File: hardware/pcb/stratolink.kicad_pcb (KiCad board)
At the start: 2 copper layers, 23.4 x 57.3 mm, 61 parts, among them J1 Solar panel direct solder, J2 Solar panel direct solder, J20 Conn_ARM_SWD_TagConnect_TC203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, J3 Conn_PinHeader_1x07_P2.54mm_V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, J4 Conn_PinHeader_1x07_P2.54mm_V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, U2 RAK3172, U5 TMP117NAIYBGR, U7 LIS2DH12TR

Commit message: Prepare v1.1 pilot hardware and verified manufacturing draft
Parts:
- added C22: 100nF, lib:Stratolink_v1p1_C22_C_0402_1005Metric, B.Cu at (55.6, 38.3)
- added R24: 4.75MΩ, lib:Stratolink_v1p1_R24_R_0402_1005Metric, B.Cu at (57.4, 33.9)
- added R25: 4.75MΩ, lib:Stratolink_v1p1_R25_R_0402_1005Metric, B.Cu at (58.6, 34.9)
- added R26: 22Ω, lib:Stratolink_v1p1_R26_R_0402_1005Metric, B.Cu at (61.2, 42.5)
- added U8: TLV8801DBVT, lib:Stratolink_v1p1_U8_SOT-23-5, B.Cu at (55.6, 36.1)
- C1: footprint Capacitor_SMD:C_0402_1005Metric -> lib:Stratolink_v1p1_C1_C_0402_1005Metric
- C10: footprint Capacitor_SMD:C_0402_1005Metric -> lib:Stratolink_v1p1_C10_C_0402_1005Metric
- C11: footprint Capacitor_SMD:C_0402_1005Metric -> lib:Stratolink_v1p1_C11_C_0402_1005Metric
- C12: footprint Capacitor_SMD:C_0402_1005Metric -> lib:Stratolink_v1p1_C12_C_0402_1005Metric
- C14: footprint Capacitor_SMD:C_0402_1005Metric -> lib:Stratolink_v1p1_C14_C_0402_1005Metric
- C15: footprint Capacitor_SMD:C_0402_1005Metric -> lib:Stratolink_v1p1_C15_C_0402_1005Metric
- C16: footprint Capacitor_SMD:C_0603_1608Metric -> lib:Stratolink_v1p1_C16_C_0603_1608Metric
- C17: footprint Capacitor_SMD:C_0402_1005Metric -> lib:Stratolink_v1p1_C17_C_0402_1005Metric
- C19: footprint Capacitor_SMD:C_0402_1005Metric -> lib:Stratolink_v1p1_C19_C_0402_1005Metric
- C2: footprint Capacitor_SMD:C_0603_1608Metric -> lib:Stratolink_v1p1_C2_C_0603_1608Metric
- C20: footprint Capacitor_SMD:C_0402_1005Metric -> lib:Stratolink_v1p1_C20_C_0402_1005Metric
- C21: footprint Capacitor_SMD:C_0603_1608Metric -> lib:Stratolink_v1p1_C21_C_0603_1608Metric
- C3: footprint Capacitor_SMD:C_0603_1608Metric -> lib:Stratolink_v1p1_C3_C_0603_1608Metric
- C4: footprint Capacitor_SMD:C_0402_1005Metric -> lib:Stratolink_v1p1_C4_C_0402_1005Metric
- C5: footprint lib:DMF4B5R5G105M3DTA0 -> lib:Stratolink_v1p1_C5_DMF4B5R5G105M3DTA0
- C6: footprint Capacitor_SMD:C_0805_2012Metric -> lib:Stratolink_v1p1_C6_C_0805_2012Metric
- C7: footprint Capacitor_SMD:C_0402_1005Metric -> lib:Stratolink_v1p1_C7_C_0402_1005Metric
- C8: footprint Capacitor_SMD:C_0603_1608Metric -> lib:Stratolink_v1p1_C8_C_0603_1608Metric
- C9: footprint Capacitor_SMD:C_0402_1005Metric -> lib:Stratolink_v1p1_C9_C_0402_1005Metric
- D1: value ESD9B3.3ST5G -> PESD5V0U1BB; footprint Diode_SMD:D_SOD-523 -> lib:Stratolink_v1p1_D1_D_SOD-523
- D3: value ESD9B3.3ST5G -> PESD5V0U1BB; footprint Diode_SMD:D_SOD-523 -> lib:Stratolink_v1p1_D3_D_SOD-523
- FB1: value ~ -> BLM15AG601SN1D; footprint Capacitor_SMD:C_0402_1005Metric -> lib:Stratolink_v1p1_FB1_C_0402_1005Metric
- J20: footprint Connector:Tag-Connect_TC2030-IDC-NL_2x03_P1.27mm_Vertical -> lib:Stratolink_v1p1_J20_Tag-Connect_TC2030-IDC-NL_2x03_P1.27mm_Vertical
- J3: value Conn_PinHeader_1x07_P2.54mm_Vertical_THT_D1mm -> Programming_1x07_P1.00mm_D0.50mm; footprint lib:Stratolink_Header_Left_1x07_P1p00_D0p50_Pad0p88 -> lib:Stratolink_Programming_Left_1x07_P1p00_D0p50_BackTack1p20x0p88
- J4: value Conn_PinHeader_1x07_P2.54mm_Vertical_THT_D1mm -> Programming_1x07_P1.00mm_D0.50mm; footprint lib:Stratolink_Header_Right_1x07_P1p00_D0p50_Pad0p88 -> lib:Stratolink_v1p1_J4_Stratolink_Programming_Right_1x07_P1p00_D0p50_BackTack1p20x0p88
- L1: footprint lib:IND_LPS4018-223MRC -> lib:Stratolink_v1p1_L1_IND_LPS4018-223MRC
- R1: value 8.25MΩ -> 7.50MΩ; footprint Resistor_SMD:R_0402_1005Metric -> lib:Stratolink_v1p1_R1_R_0402_1005Metric
- R10: footprint Resistor_SMD:R_0402_1005Metric -> lib:Stratolink_v1p1_R10_R_0402_1005Metric
- R11: footprint Resistor_SMD:R_0402_1005Metric -> lib:Stratolink_v1p1_R11_R_0402_1005Metric
- R12: footprint Resistor_SMD:R_0402_1005Metric -> lib:Stratolink_v1p1_R12_R_0402_1005Metric
- R13: footprint Resistor_SMD:R_0402_1005Metric -> lib:Stratolink_v1p1_R13_R_0402_1005Metric
- R14: footprint Resistor_SMD:R_0402_1005Metric -> lib:Stratolink_v1p1_R14_R_0402_1005Metric
- R15: footprint Resistor_SMD:R_0402_1005Metric -> lib:Stratolink_v1p1_R15_R_0402_1005Metric
- R16: footprint Resistor_SMD:R_0402_1005Metric -> lib:Stratolink_v1p1_R16_R_0402_1005Metric
- R18: footprint Resistor_SMD:R_0402_1005Metric -> lib:Stratolink_v1p1_R18_R_0402_1005Metric
- R19: footprint Resistor_SMD:R_0402_1005Metric -> lib:Stratolink_v1p1_R19_R_0402_1005Metric
- R2: footprint Resistor_SMD:R_0402_1005Metric -> lib:Stratolink_v1p1_R2_R_0402_1005Metric
- R21: footprint Resistor_SMD:R_0402_1005Metric -> lib:Stratolink_v1p1_R21_R_0402_1005Metric
- R22: footprint Resistor_SMD:R_0402_1005Metric -> lib:Stratolink_v1p1_R22_R_0402_1005Metric
- R23: footprint Resistor_SMD:R_0402_1005Metric -> lib:Stratolink_v1p1_R23_R_0402_1005Metric
- R3: footprint Resistor_SMD:R_0402_1005Metric -> lib:Stratolink_v1p1_R3_R_0402_1005Metric
- R4: footprint Resistor_SMD:R_0402_1005Metric -> lib:Stratolink_v1p1_R4_R_0402_1005Metric
- R5: footprint Resistor_SMD:R_0402_1005Metric -> lib:Stratolink_v1p1_R5_R_0402_1005Metric
- R6: footprint Resistor_SMD:R_0402_1005Metric -> lib:Stratolink_v1p1_R6_R_0402_1005Metric
- R7: footprint Resistor_SMD:R_0402_1005Metric -> lib:Stratolink_v1p1_R7_R_0402_1005Metric
- R8: footprint Resistor_SMD:R_0402_1005Metric -> lib:Stratolink_v1p1_R8_R_0402_1005Metric
- R9: footprint Resistor_SMD:R_0402_1005Metric -> lib:Stratolink_v1p1_R9_R_0402_1005Metric
- U1: value ~ -> BQ25570RGRR; footprint lib:QFN50P350X350X100-21N -> lib:Stratolink_v1p1_U1_QFN50P350X350X100-21N
- U2: value RAK3172 -> RAK3172-9-SM-NI; footprint lib:RAK3172 -> lib:Stratolink_v1p1_U2_RAK3172
- U3: value ~ -> MAX-M10S-00B; footprint lib:XCVR_MAX-M10S-00B -> lib:Stratolink_v1p1_U3_XCVR_MAX-M10S-00B
- U4: value ~ -> MS561101BA03-50; footprint lib:SON125P500X300X100-8N -> lib:Stratolink_v1p1_U4_SON125P500X300X100-8N
- U5: value TMP117NAIYBGR -> TMP117AIYBGR; footprint lib:BGA6N40P3X2_148X95X53 -> lib:Stratolink_v1p1_U5_BGA6N40P3X2_148X95X53
- U6: value ~ -> LTR-390UV-01; footprint lib:SMD6_LTR-390UV-01_LTO-L -> lib:Stratolink_v1p1_U6_SMD6_LTR-390UV-01_LTO-L
- U7: footprint lib:PQFN50P200X200100-12N -> lib:Stratolink_v1p1_U7_PQFN50P200X200100-12N
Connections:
- net Net-(U1-VBAT) renamed /VBAT
- C5 pad 3: (no net) -> /SC_MID
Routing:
- net /SC_MID: track 0.00 -> 22.1 mm, vias 0 -> 2
- net GND: track 246.0 -> 263.4 mm
- net /SC_BAL_OUT: track 0.00 -> 15.4 mm, vias 0 -> 2
- net /VBAT: track 11.7 -> 27.0 mm, vias 0 -> 2
- net VSTOR: track 103.9 -> 95.3 mm, vias 6 -> 7
- net /SC_HALF_REF: track 0.00 -> 4.62 mm
- net SCL: track 96.5 -> 97.6 mm
- net +3.3V: track 142.3 -> 142.9 mm, vias 7 -> 8

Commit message: Resolve v1.1 pilot sourcing and document multiband UV options
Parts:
- U2: value RAK3172-9-SM-NI -> RAK3172-8-SM-NI
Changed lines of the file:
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@@
 			)
 		)
-		(property "Value" "RAK3172-9-SM-NI"
+		(property "Value" "RAK3172-8-SM-NI"
 			(at 0 0 0)
 			(layer "F.Fab")
@@
 			)
 		)
-		(property "Datasheet" ""
+		(property "Datasheet" "https://docs.rakwireless.com/product-categories/wisduo/rak3172-module/datasheet/"
 			(at 0 0 0)
 			(layer "F.Fab")
@@
 			)
 		)
-		(property "Description" "RAK3172-9-SM-NI sub-GHz STM32WLE5CC radio module"
+		(property "Description" "RAK3172 STM32WLE5CC, 32-pad, high-band regional-label variant, no TCXO, no IPEX; antenna on RF pad 12"
 			(at 0 0 0)
 			(layer "F.Fab")
@@
 			)
 		)
-		(property "DESCRIPTION" "RAK3172-9-SM-NI sub-GHz STM32WLE5CC radio module"
+		(property "DESCRIPTION" "RAK3172 STM32WLE5CC, 32-pad, high-band regional-label variant, no TCXO, no IPEX; antenna on RF pad 12"
 			(at 0 0 180)
 			(unlocked yes)
@@
 			)
 		)
-		(property "MP" "RAK3172-9-SM-NI"
+		(property "MP" "RAK3172-8-SM-NI"
 			(at 0 0 180)
 			(unlocked yes)
@@
 			)
 		)
-		(property "Description_1" "RAK3172-9-SM-NI sub-GHz STM32WLE5CC radio module"
+		(property "Description_1" "RAK3172 STM32WLE5CC, 32-pad, high-band regional-label variant, no TCXO, no IPEX; antenna on RF pad 12"
 			(at 0 0 180)
 			(unlocked yes)
@@
 			)
 		)
-		(property "Availability" "Not in stock"
+		(property "Availability" ""
 			(at 0 0 180)
 			(unlocked yes)
@@
 			)
 		)
-		(property "AVAILABILITY" "Not in stock"
+		(property "AVAILABILITY" ""
 			(at 0 0 180)
 			(unlocked yes)
@@
 			)
 		)
-		(property "Manufacturer_Part_Number" "RAK3172-9-SM-NI"
+		(property "Manufacturer_Part_Number" "RAK3172-8-SM-NI"
 			(at 0 0 0)
 			(layer "F.Fab")
@@
 			)
 		)
-		(property "LCSC" "C18548052"
+		(property "LCSC" "C5452091"
 			(at 0 0 0)
 			(layer "F.Fab")
@@
 			)
 		)
-		(property "Supplier Part" "C18548052"
+		(property "Supplier Part" "C5452091"
 			(at 0 0 0)
 			(layer "F.Fab")
@@
 			)
 		)
-		(property "Datasheet" "https://www.lcsc.com/product-detail/C2766827.html"
+		(property "Datasheet" "https://yageogroup.com/content/datasheet/asset/file/PYU-RC_GROUP_51_ROHS_L"
 			(at 0 0 270)
 			(unlocked yes)
@@
 			)
 		)
-		(property "Description" "0402WGF3654TCE"
+		(property "Description" "3.65 MΩ, ±1%, ±100 ppm/°C, 0402, 62.5 mW, 50 V thick-film resistor"
 			(at 0 0 270)
 			(unlocked yes)
@@
 			)
 		)
-		(property "Manufacturer" "UNI-ROYAL"
+		(property "Manufacturer" "YAGEO"
 			(at 0 0 0)
 			(layer "F.Fab")
@@
 			)
 		)
-		(property "Manufacturer_Part_Number" "0402WGF3654TCE"
+		(property "Manufacturer_Part_Number" "RC0402FR-073M65L"
 			(at 0 0 0)
 			(layer "F.Fab")
@@
 			)
 		)
-		(property "LCSC" "C2766827"
+		(property "LCSC" "C477700"
 			(at 0 0 0)
 			(layer "F.Fab")
@@
 			)
 		)
-		(property "Supplier Part" "C2766827"
+		(property "Supplier Part" "C477700"
 			(at 0 0 0)
 			(layer "F.Fab")

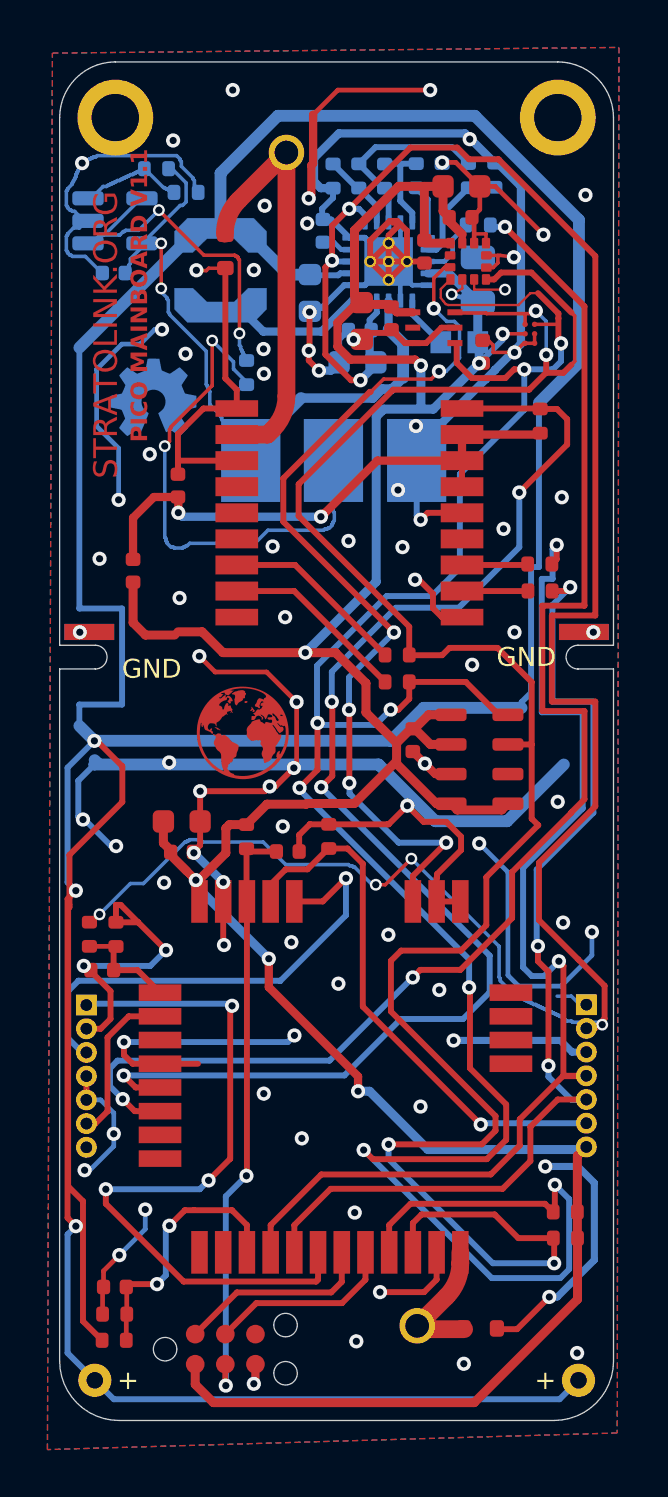
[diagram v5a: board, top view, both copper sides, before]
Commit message: Complete AS7331 v1.1 layout and green-mask pilot package
Replace the UV circuit with the reviewed AS7331 design, restore selective
green solder mask without silkscreen, and retain a U6-only DNP pilot
assembly and stencil variant. Add the quiet UV-DNP firmware target.

Record independent electrical, geometry, mask and population checks,
and the saved JLC cart for five PCBs with three assembled pilots.
Factory CAM and physical qualification remain pending; no order placed.
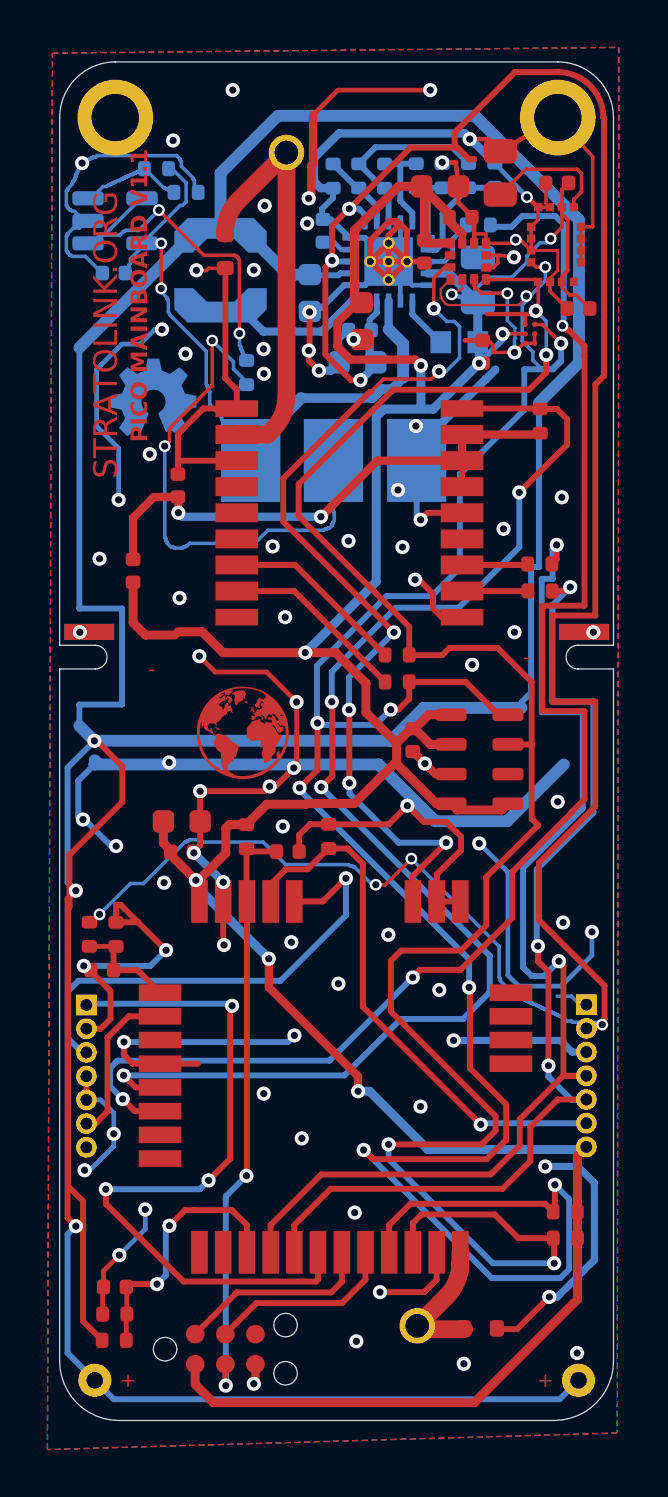
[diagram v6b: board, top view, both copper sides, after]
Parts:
- added C23: 100nF, lib:Stratolink_v1p1_C23_C_0402_1005Metric, F.Cu at (75.2, 39.8)
- added R27: 3.3MΩ, lib:Stratolink_v1p1_R27_R_0805_2012Metric, F.Cu at (71.9, 34.1)
- U6: value LTR-390UV-01 -> AS7331-AQFM; footprint lib:Stratolink_v1p1_U6_SMD6_LTR-390UV-01_LTO-L -> lib:Stratolink_v1p1_U6_AS7331_OLGA16
- moved C14 9.02 mm to (74.3, 34.5), turned to 0 degrees
- moved U6 6.23 mm to (74.2, 37.1)
- moved C21 0.90 mm to (69.4, 34.6)
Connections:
- U6 pad 1: +3.3V -> GND
- U6 pad 2: unconnected-(U6-NC-Pad2) -> GND
- U6 pad 3: GND -> +3.3V
- U6 pad 4: SCL -> /UV_REXT
- U6 pad 6: SDA -> GND
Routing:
- net GND: track 263.4 -> 273.3 mm
- net +3.3V: track 142.9 -> 152.7 mm, vias 8 -> 9
- net VSTOR: track 95.3 -> 104.4 mm
- net /UV_REXT: track 0.00 -> 5.50 mm
- net SDA: track 91.0 -> 87.3 mm
- net PB5: track 58.9 -> 60.9 mm
- net SCL: track 97.6 -> 99.1 mm, vias 8 -> 9
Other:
- board text added: "-"
- board text removed: "GND"

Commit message: Round copper junctions and close fabrication pockets
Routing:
- net GND: track 273.3 -> 275.5 mm
- net /SC_BAL_OUT: track 15.4 -> 16.3 mm

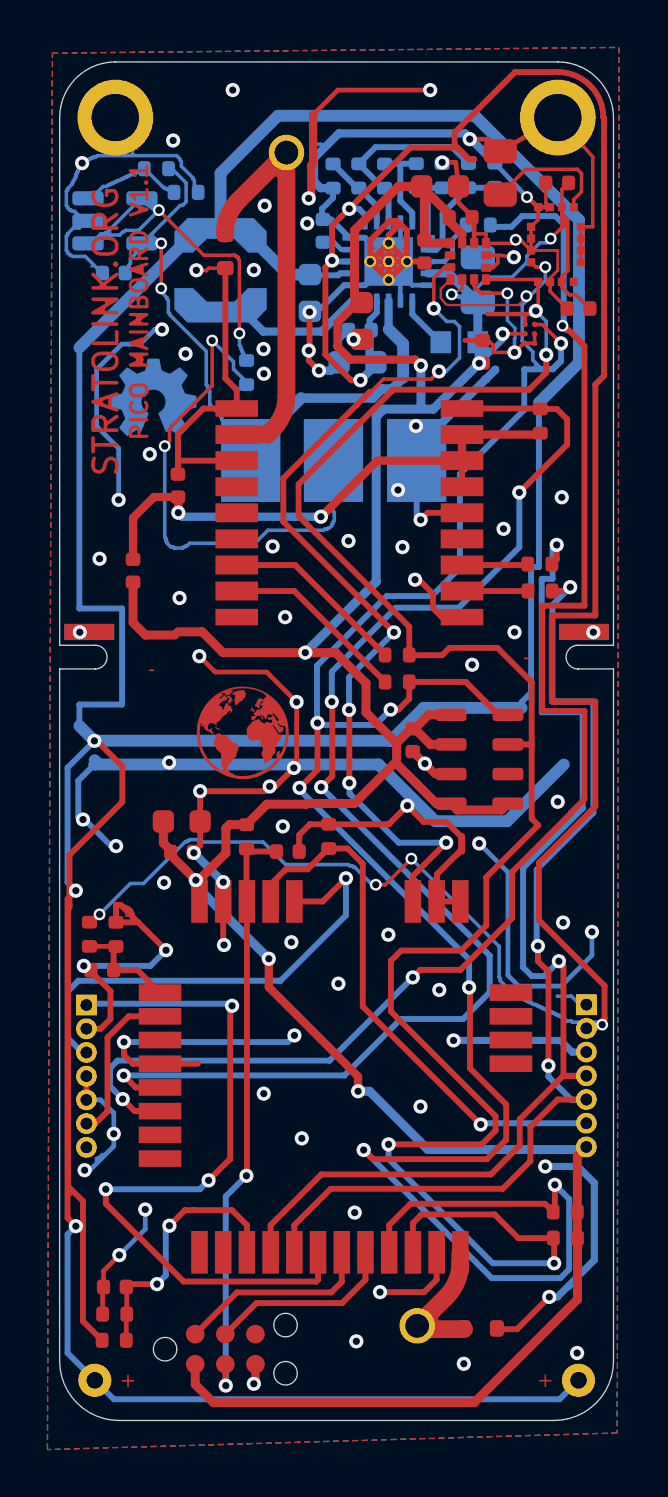
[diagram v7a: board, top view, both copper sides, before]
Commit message: Move GNSS feed clear of switching copper and restore ground reference
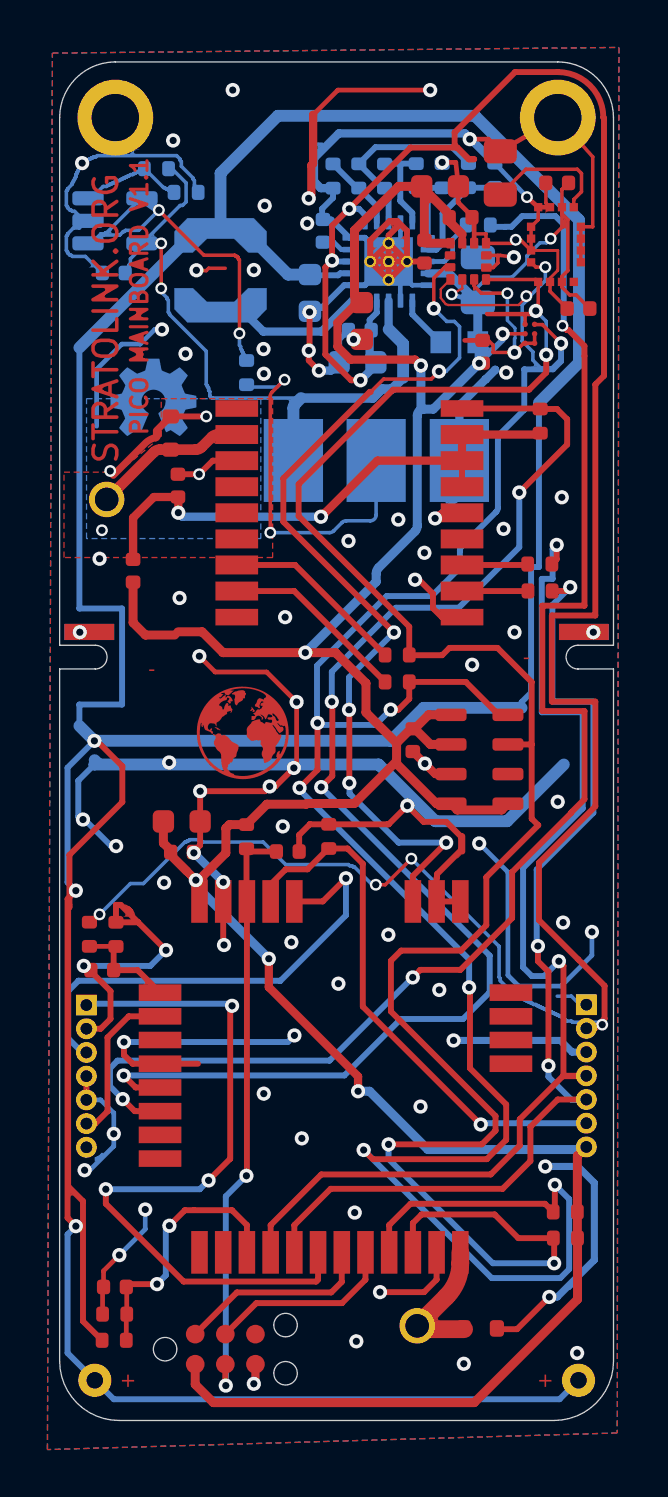
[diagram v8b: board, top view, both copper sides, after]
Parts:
- moved AE2 16.5 mm to (55.3, 47.9), turned to 180 degrees
- moved D3 8.00 mm to (58.0, 45.0), turned to -90 degrees
- moved C5 1.80 mm to (66.7, 64.7)
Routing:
- net GND: track 275.5 -> 261.6 mm, vias 85 -> 86
- net Net-(AE2-A): track 17.8 -> 6.57 mm
- net /SC_MID: track 22.1 -> 15.5 mm
- net /VBAT: track 27.0 -> 28.9 mm
- net +3.3V: track 152.9 -> 151.9 mm
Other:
- board text added: "GNSS: 48 mm straight wire LEFT from feed; tune assembled payload"
